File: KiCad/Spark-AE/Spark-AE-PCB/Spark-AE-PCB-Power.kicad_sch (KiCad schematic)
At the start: 7 parts, among them J5 AE_BUS

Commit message: assigned footprints & sorted ratsnest
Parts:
- added C2: 220uF, Capacitor_SMD:CP_Elec_6.3x5.4, symbol Device:C_Polarized_US
- C1: renamed from C10; value 470uF -> 220uF; footprint (none) -> Capacitor_SMD:CP_Elec_6.3x5.4
- C3: renamed from C11; footprint (none) -> Capacitor_SMD:C_0805_2012Metric
- C4: renamed from C12; footprint (none) -> Capacitor_SMD:C_0805_2012Metric
- D1: value 1N5817 -> SS14; footprint (none) -> Diode_SMD:D_SMA
- FB1: footprint (none) -> Inductor_SMD:L_0603_1608Metric
- NT1: footprint (none) -> NetTie:NetTie-3_SMD_Pad2.0mm
- renumbered J5 to J3
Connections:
- net +5V: now also C2.1
- net GND: now also C2.2
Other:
- moved on the sheet: C1

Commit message: schematic 100% complete. pcb layout around 50% complete.
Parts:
- removed D1: SS14, Diode_SMD:D_SMA, symbol Device:D_Schottky
- removed NT1: NetTie_3_Tee, NetTie:NetTie-3_SMD_Pad2.0mm, symbol Device:NetTie_3_Tee
- added C3, C5, C7: 100nF, Capacitor_SMD:C_0805_2012Metric, symbol Device:C
- added Q1: AO3401, Package_TO_SOT_SMD:SOT-23, symbol Transistor_FET:Q_PMOS_GSD
- C1: value 220uF -> 100uF; footprint Capacitor_SMD:CP_Elec_6.3x5.4 -> Capacitor_SMD:C_0805_2012Metric; symbol Device:C_Polarized_US -> Device:C
- C2: value 220uF -> 10uF; footprint Capacitor_SMD:CP_Elec_6.3x5.4 -> Capacitor_SMD:C_0805_2012Metric; symbol Device:C_Polarized_US -> Device:C
- FB1: value BLM18AG601 -> FerriteBead; footprint Inductor_SMD:L_0603_1608Metric -> Inductor_SMD:L_0805_2012Metric
- renumbered C3 to C4, C4 to C6
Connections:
- net +5V: now also C3.1; no longer J3.1 (Pin_1), J3.2 (Pin_2)
- net GND: now also C3.2, C5.2, C7.2, Q1.1 (G); no longer FB1.2
- net GNDA: no longer names the net of C6.2
- net GNDA: now also C7.1
- net GNDD: no longer names the net of C4.2
- net GNDD: now also C5.1
- new net VCC_PROTECT: FB1.2, Q1.2 (S)
- new net VCC_RAW: J3.1 (Pin_1), J3.2 (Pin_2), Q1.3 (D)
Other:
- note added: "Power Regulation"
- moved on the sheet: C4, C6, J3

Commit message: continuing to plug away at pcb layout
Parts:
- removed C6: 10uF, Capacitor_SMD:C_0805_2012Metric, symbol Device:C
- removed C7: 100nF, Capacitor_SMD:C_0805_2012Metric, symbol Device:C
- C4: footprint Capacitor_SMD:C_0805_2012Metric -> Capacitor_SMD:C_0603_1608Metric
- C5: value 100nF -> 10uF; footprint Capacitor_SMD:C_0805_2012Metric -> Capacitor_SMD:C_0603_1608Metric
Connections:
- net +3.3V: now also C4.2; no longer C4.1
- net +3.3VA: now also C5.2
- net GND: now also C4.1, C5.1; no longer C5.2
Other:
- moved on the sheet: C4

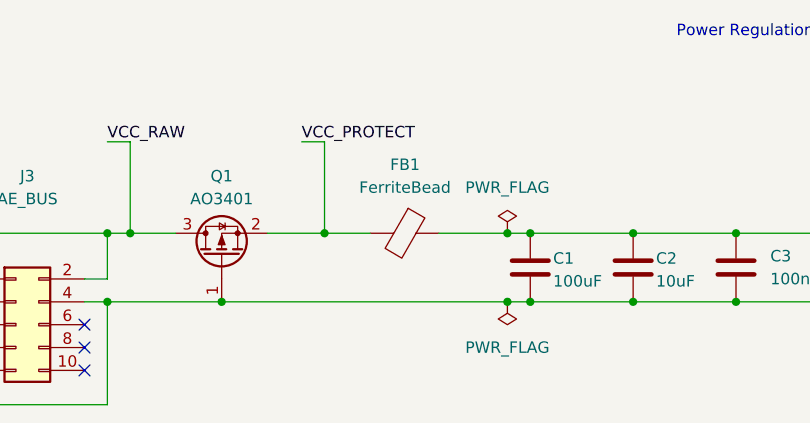
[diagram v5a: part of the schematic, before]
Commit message: mk0 prototype sent for production! commit includes a couple of necessary tweaks.
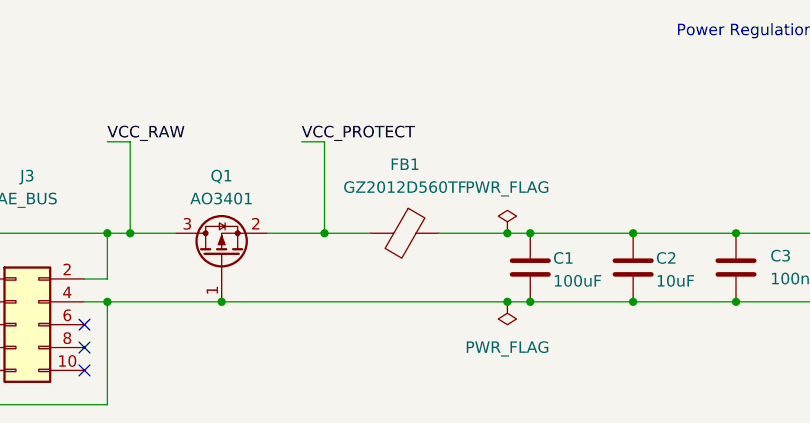
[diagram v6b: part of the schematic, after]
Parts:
- FB1: value FerriteBead -> GZ2012D560TF
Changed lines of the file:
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@@
 			)
 		)
-		(property "Value" "FerriteBead"
+		(property "Value" "GZ2012D560TF"
 			(at 92.7608 86.36 90)
 			(show_name no)
